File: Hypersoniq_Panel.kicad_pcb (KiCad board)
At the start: 2 copper layers, 40.4 x 128.5 mm, 13 parts

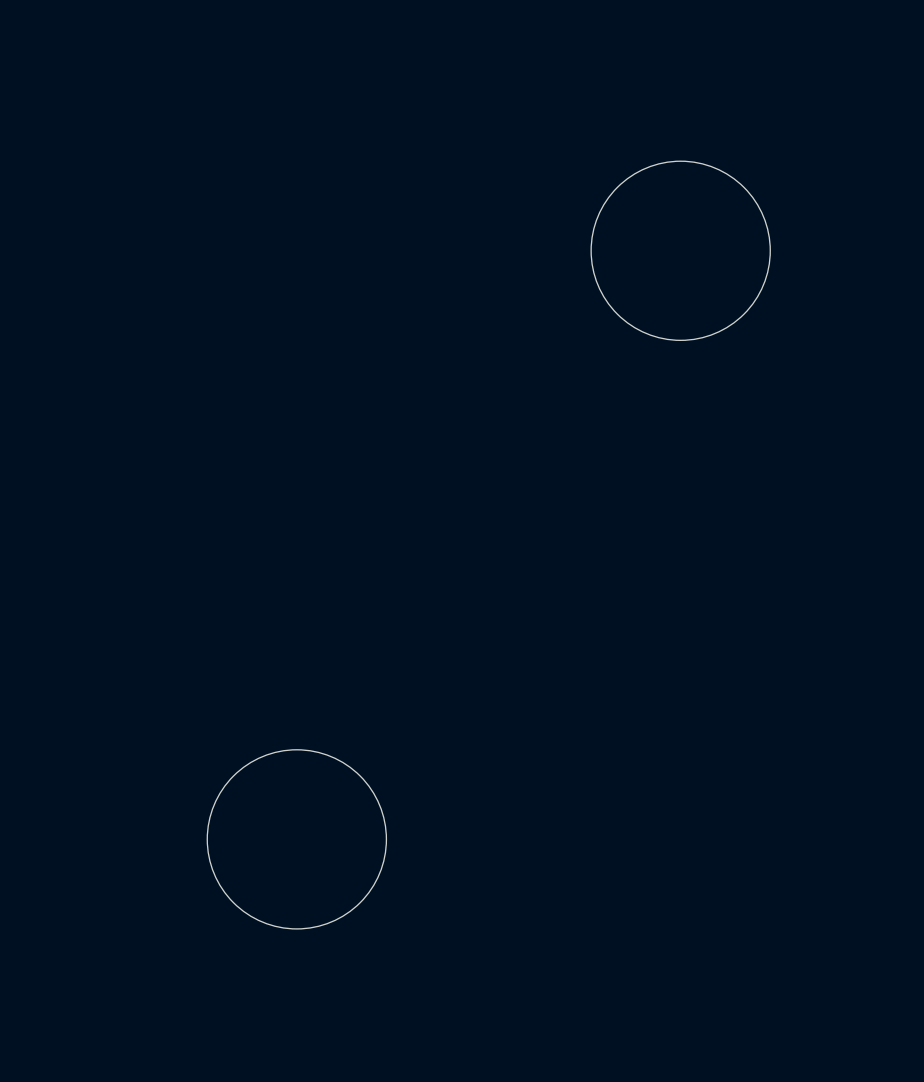
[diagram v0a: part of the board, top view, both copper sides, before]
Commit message: Started generating JLC placement details
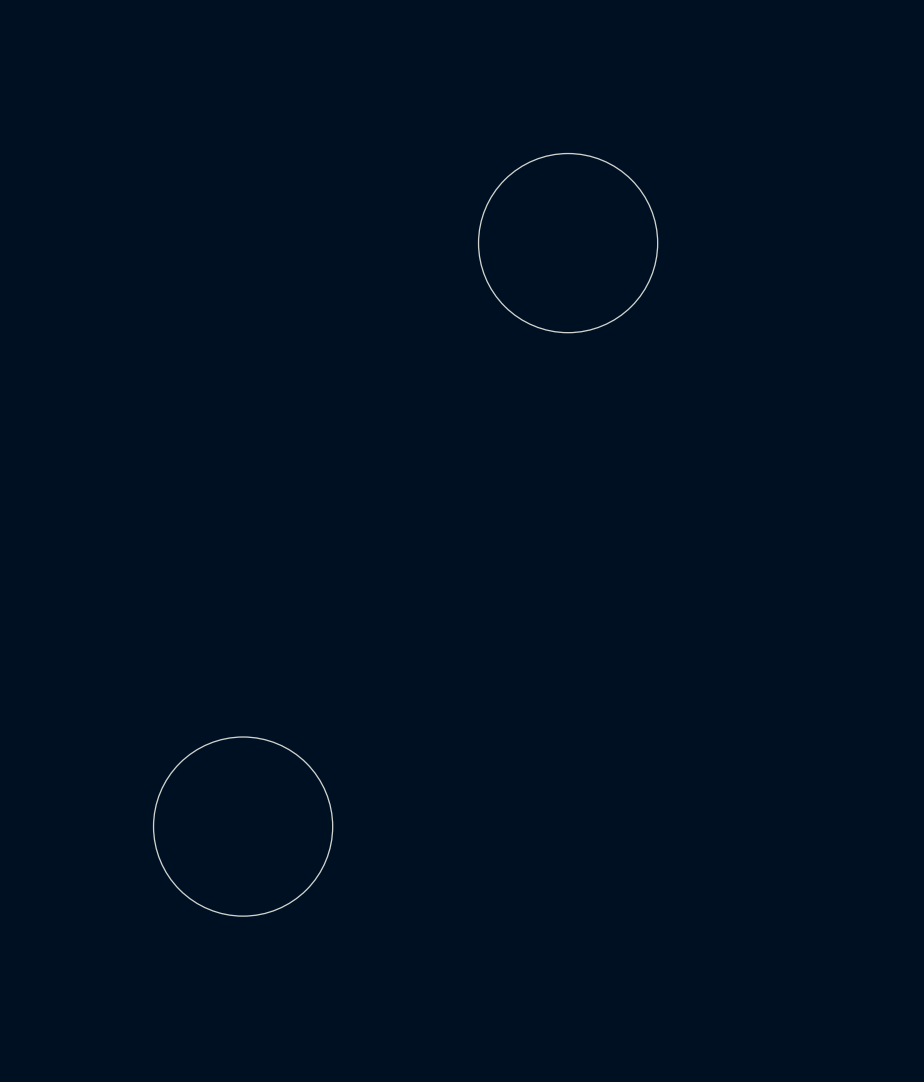
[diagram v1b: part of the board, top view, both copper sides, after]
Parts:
- removed G***: LOGO, Graphics:logo
- added kibuzzard-64BD36C9: G***, kibuzzard-64BD36C9, F.Cu at (57.8, 148.5)
- added kibuzzard-64BD3725: G***, kibuzzard-64BD3725, F.Cu at (83.1, 148.4)
- added kibuzzard-64BD3DD7: G***, kibuzzard-64BD3DD7, F.Cu at (70.2, 153.3)
- added kibuzzard-64BD4829: G***, kibuzzard-64BD4829, F.Cu at (79.8, 84.3)
- added kibuzzard-64BD5372: G***, kibuzzard-64BD5372, F.Cu at (70.6, 83.9)
- moved kibuzzard-63FBCCA9 5.50 mm to (55.6, 91.3)
- moved Ref** 4.41 mm to (75.6, 53.3)
- moved Ref** 2.16 mm to (62.9, 76.1)
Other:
- board text added: "HYPERSONIQ"

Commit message: Panel and Control tidy up
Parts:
- removed kibuzzard-64BD3DD7: G***, kibuzzard-64BD3DD7
- removed kibuzzard-64BD4829: G***, kibuzzard-64BD4829
- added kibuzzard-64BFAFE6: G***, kibuzzard-64BFAFE6, F.Cu at (79.8, 80.9)
- added kibuzzard-64BFB036: G***, kibuzzard-64BFB036, F.Cu at (70.2, 152.4)
- moved kibuzzard-63FBCCA9 0.50 mm to (56.1, 91.3)
- moved PWM_In 0.10 mm to (80.0, 104.0)

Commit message: v1.0 Design sent for manufacture
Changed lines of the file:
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@@
     (pad_to_mask_clearance 0)
     (pcbplotparams
-      (layerselection 0x00010fc_ffffffff)
+      (layerselection 0x00010f0_ffffffff)
       (plot_on_all_layers_selection 0x0000000_00000000)
       (disableapertmacros false)
@@
       (drillshape 0)
       (scaleselection 1)
-      (outputdirectory "Gerbers/Panel/")
+      (outputdirectory "Gerbers/Hypersoniq_Panel/")
     )
   )
@@
     (attr board_only exclude_from_pos_files exclude_from_bom)
     (fp_text reference "kibuzzard-64BFB036" (at 0 -5.432247 90) (layer "F.SilkS") hide
-        (effects (font (size 0 0)))
+        (effects (font (size 0 0) (thickness 0.15)))
     )
     (fp_text value "G***" (at 0 5.432247 90) (layer "F.SilkS") hide
-        (effects (font (size 0 0)))
+        (effects (font (size 0 0) (thickness 0.15)))
     )
     (fp_poly
@@
     (fp_arc (start -7.88 8.32) (mid -8.081749 8.227632) (end -8.16 8.02)
       (stroke (width 0.12) (type solid)) (layer "Edge.Cuts"))
-    (fp_arc (start 7.88 -8.32) (mid 8.096588 -8.233658) (end 8.19 -8.02)
+    (fp_arc (start 7.88 -8.32) (mid 8.096622 -8.233665) (end 8.19 -8.02)
       (stroke (width 0.12) (type solid)) (layer "Edge.Cuts"))
     (fp_arc (start 8.19 8.02) (mid 8.100917 8.238111) (end 7.88 8.32)
@@
     (fp_arc (start -7.88 8.32) (mid -8.081749 8.227632) (end -8.16 8.02)
       (stroke (width 0.12) (type solid)) (layer "Edge.Cuts"))
-    (fp_arc (start 7.88 -8.32) (mid 8.096588 -8.233658) (end 8.19 -8.02)
+    (fp_arc (start 7.88 -8.32) (mid 8.096622 -8.233665) (end 8.19 -8.02)
       (stroke (width 0.12) (type solid)) (layer "Edge.Cuts"))
     (fp_arc (start 8.19 8.02) (mid 8.100917 8.238111) (end 7.88 8.32)
@@
     (fp_arc (start -7.88 8.32) (mid -8.081749 8.227632) (end -8.16 8.02)
       (stroke (width 0.12) (type solid)) (layer "Edge.Cuts"))
-    (fp_arc (start 7.88 -8.32) (mid 8.096588 -8.233658) (end 8.19 -8.02)
+    (fp_arc (start 7.88 -8.32) (mid 8.096622 -8.233665) (end 8.19 -8.02)
       (stroke (width 0.12) (type solid)) (layer "Edge.Cuts"))
     (fp_arc (start 8.19 8.02) (mid 8.100917 8.238111) (end 7.88 8.32)
@@
     (fp_arc (start -7.88 8.32) (mid -8.081749 8.227632) (end -8.16 8.02)
       (stroke (width 0.12) (type solid)) (layer "Edge.Cuts"))
-    (fp_arc (start 7.88 -8.32) (mid 8.096588 -8.233658) (end 8.19 -8.02)
+    (fp_arc (start 7.88 -8.32) (mid 8.096622 -8.233665) (end 8.19 -8.02)
       (stroke (width 0.12) (type solid)) (layer "Edge.Cuts"))
     (fp_arc (start 8.19 8.02) (mid 8.100917 8.238111) (end 7.88 8.32)
@@
     (attr board_only exclude_from_pos_files exclude_from_bom)
     (fp_text reference "kibuzzard-64BFAFE6" (at 0 -5.294375 90) (layer "F.SilkS") hide
-        (effects (font (size 0 0)))
+        (effects (font (size 0 0) (thickness 0.15)))
     )
     (fp_text value "G***" (at 0 5.294375 90) (layer "F.SilkS") hide
-        (effects (font (size 0 0)))
-    )
-    (fp_poly
+        (effects (font (size 0 0) (thickness 0.15)))
+    )
+    (fp_poly
